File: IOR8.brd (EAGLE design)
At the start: 62.2 x 46.7 mm, 55 parts, among them Q1 2N7002, Q2 2N7002, Q3 2N7002, Q4 2N7002, Q5 2N7002, Q6 2N7002, Q7 2N7002, Q8 2N7002

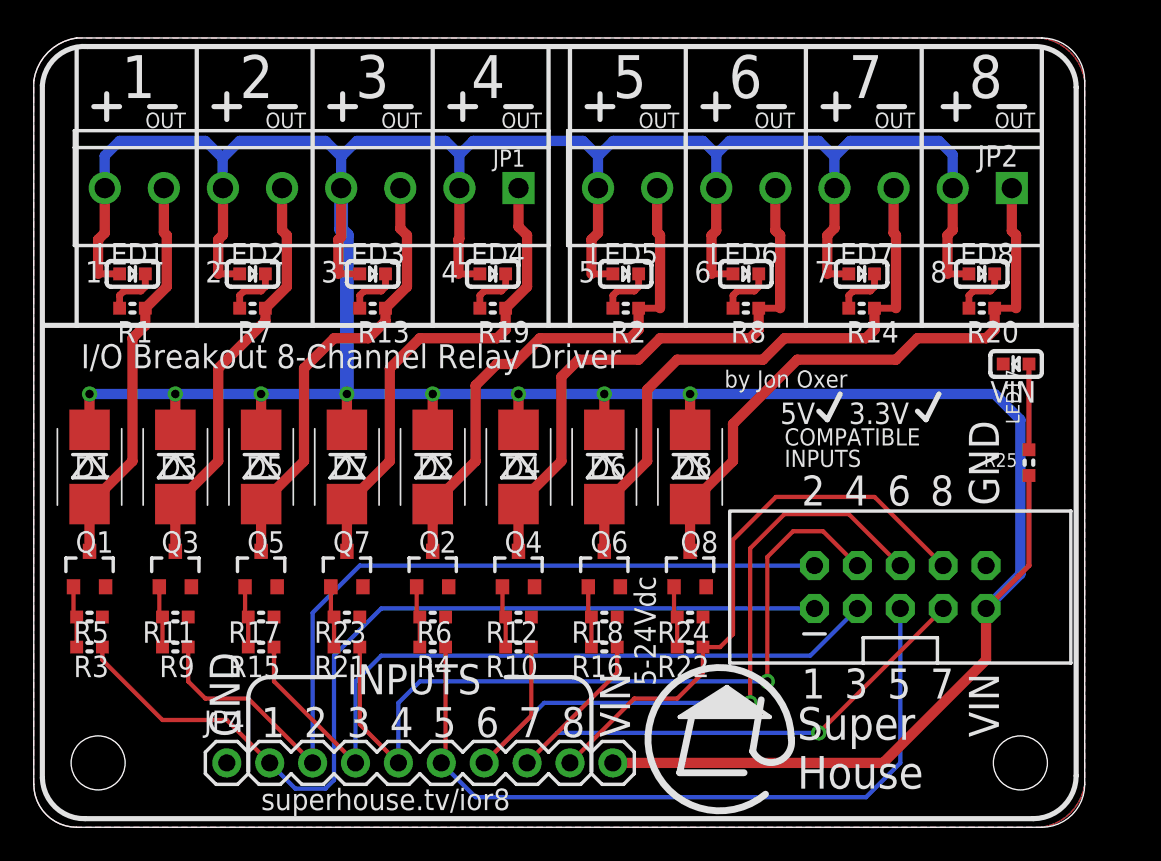
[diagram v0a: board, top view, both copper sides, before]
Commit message: Expanded headers to 2x6 to include IOREF and RESET for v2.0 release
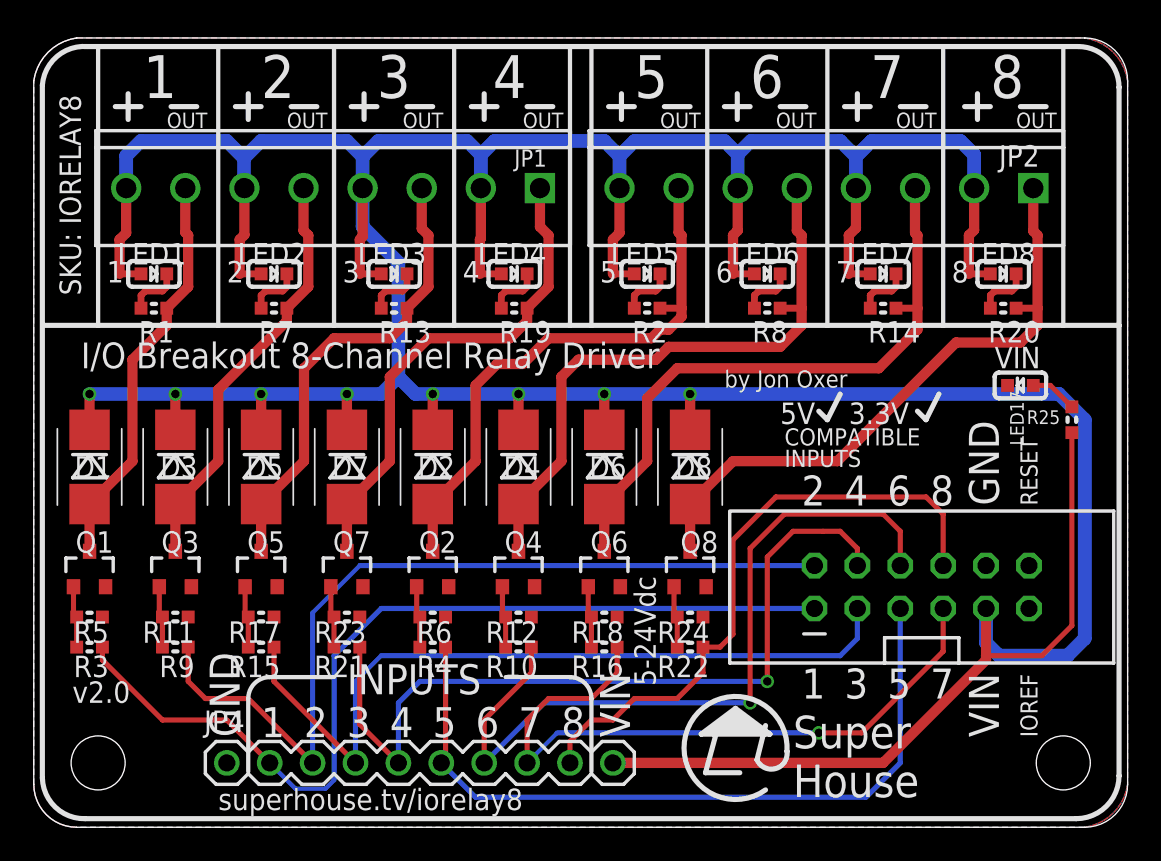
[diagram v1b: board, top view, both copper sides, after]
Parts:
- JP3: value M05X2SHD -> M06X2; device freetronics-original:2X5-SHROUDED -> freetronics-jon:2X6-SHROUDED
- moved JP3 5.24 mm to (46.2, 13.0)
- moved U$6 4.02 mm to (15.2, 29.3)
- moved R25 3.59 mm to (61.5, 24.1)
- moved LED17 1.30 mm to (58.4, 26.2)
- moved JP2 1.27 mm to (59.2, 37.8)
- moved LED5 1.27 mm to (36.3, 32.8)
- moved LED7 1.27 mm to (50.3, 32.8)
- moved LED8 1.27 mm to (57.4, 32.8)
- moved R14 1.27 mm to (50.3, 30.7)
- moved R2 1.27 mm to (36.3, 30.7)
- moved R20 1.27 mm to (57.4, 30.7)
- moved LED1 1.27 mm to (7.11, 32.8)
- moved R1 1.27 mm to (7.11, 30.7)
- moved JP1 1.27 mm to (30.0, 37.8)
- moved LED2 1.27 mm to (14.2, 32.8)
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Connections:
- new net IOREF: JP3.11
- new net RESET: JP3.12
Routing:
- net VCC: track 256.1 -> 278.3 mm
- net D6: track 37.5 -> 40.5 mm
- net D7: track 34.5 -> 37.0 mm
- net N$15: track 34.0 -> 36.4 mm
- net N$4: track 5.08 -> 2.81 mm
- net N$17: track 35.4 -> 37.6 mm
- net N$13: track 31.6 -> 33.7 mm
- net N$9: track 26.6 -> 27.9 mm
- net D5: track 45.4 -> 46.6 mm
- net N$19: track 36.2 -> 37.3 mm
- net D2: track 45.2 -> 46.2 mm
- net N$11: track 29.0 -> 29.7 mm
- net D3: track 47.9 -> 48.5 mm
- net N$5: track 23.5 -> 24.0 mm
- net N$3: track 24.5 -> 25.1 mm
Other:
- board size 62.2 x 46.7 mm -> 64.8 x 46.7 mm
- board text added: "(c) 2017 SuperHouse Automation"
- board text added: "IOREF"
- board text added: "RESET"
- board text added: "SKU: IORELAY8"
- board text added: "superhouse.tv/iorelay8"
- board text added: "v2.0"
- board text removed: "(c) 2017 SuperHouse Pty Ltd"
- board text removed: "ROHS"
- board text removed: "SKU: IOR8"
- board text removed: "superhouse.tv/ior8"
